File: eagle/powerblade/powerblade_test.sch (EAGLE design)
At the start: 78 parts, among them J1 JTAG_14PIN_IDC-NL, J21 AC_INFILM, Q1 2N7002, U1 TPS62122, U2 AD524, U3 MSP430FR5738, U4 LTC5800, U5 MAX9910, U6 MAX9910

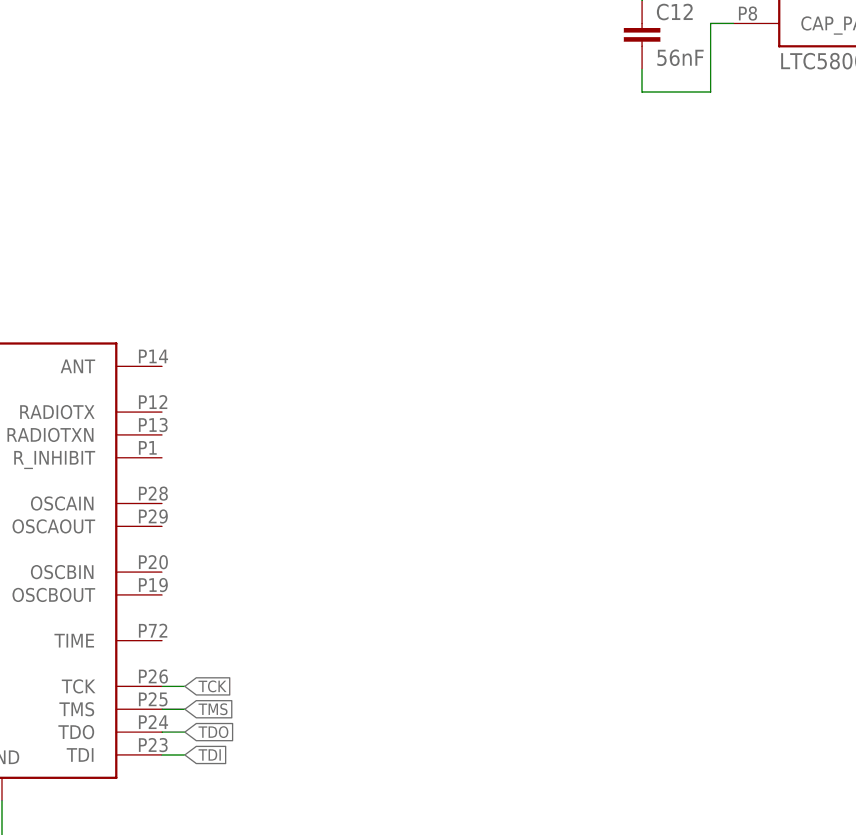
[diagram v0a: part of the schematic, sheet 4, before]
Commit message: added crystals to ltc5800 sch in powerblade test
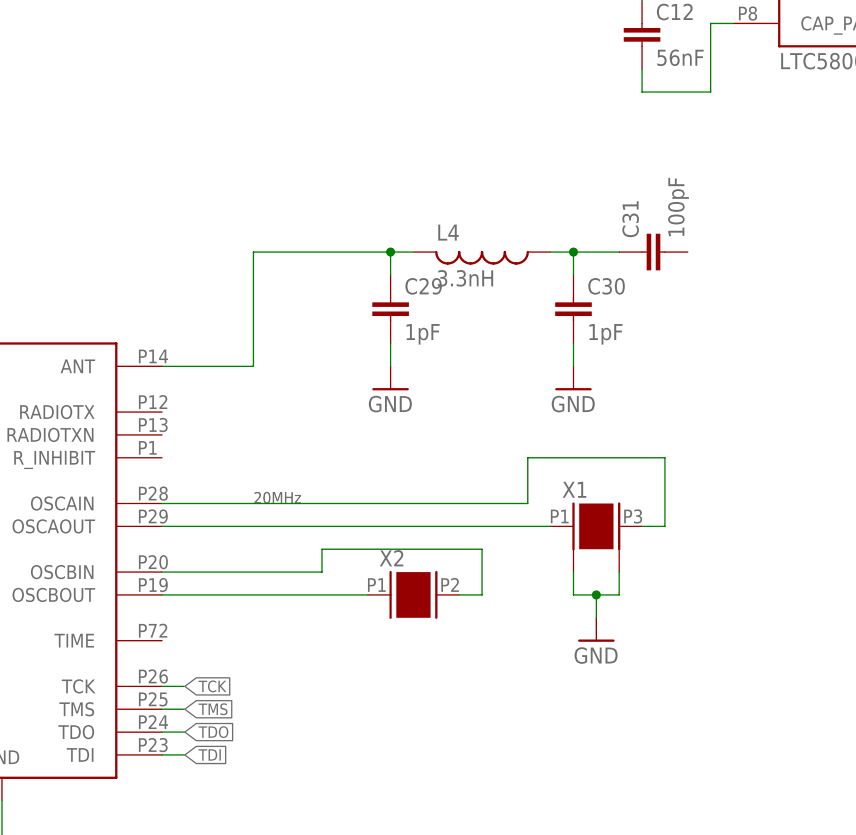
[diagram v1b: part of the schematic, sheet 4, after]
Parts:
- added C29, C30: 1pF, rcl:C-EUC0201
- added C31: 100pF, rcl:C-EUC0201
- added L4: 3.3nH, rcl:L-USL0201
- added X1: ABM8G, powerfilm:ABM8G
- added X2: ABS07, powerfilm:ABS07
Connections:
- new net N$42: U4G$2.OSCAOUT, X1.P1
- new net N$43: U4G$2.OSCAIN, X1.P2
- new net N$44: U4G$2.OSCBIN, X2.P2
- new net N$45: U4G$2.OSCBOUT, X2.P1
- new net N$46: C29.1, L4.2, U4G$2.ANT
- new net N$47: C30.1, C31.1, L4.1
- net GND: now also C29.2, C30.2, X1.G1, X1.G2
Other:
- note added: "20MHz"
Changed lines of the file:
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@@
 <part name="GND32" library="supply1" deviceset="GND" device=""/>
 <part name="+3V9" library="supply1" deviceset="+3V3" device=""/>
+<part name="X1" library="powerfilm" deviceset="ABM8G" device=""/>
+<part name="GND33" library="supply1" deviceset="GND" device=""/>
+<part name="X2" library="powerfilm" deviceset="ABS07" device=""/>
+<part name="L4" library="rcl" deviceset="L-US" device="L0201" value="3.3nH"/>
+<part name="C29" library="rcl" deviceset="C-EU" device="C0201" value="1pF"/>
+<part name="C30" library="rcl" deviceset="C-EU" device="C0201" value="1pF"/>
+<part name="C31" library="rcl" deviceset="C-EU" device="C0201" value="100pF"/>
+<part name="GND34" library="supply1" deviceset="GND" device=""/>
+<part name="GND35" library="supply1" deviceset="GND" device=""/>
 </parts>
 <sheets>
@@
 <description>Load 2: LTC5800</description>
 <plain>
+<text x="27.94" y="0" size="1.27" layer="97">20MHz</text>
 </plain>
 <instances>
@@
 <instance part="GND32" gate="1" x="2.54" y="-93.98"/>
 <instance part="+3V9" gate="G$1" x="-149.86" y="25.4"/>
+<instance part="X1" gate="G$1" x="66.04" y="-2.54"/>
+<instance part="GND33" gate="1" x="66.04" y="-15.24"/>
+<instance part="X2" gate="G$1" x="45.72" y="-10.16"/>
+<instance part="L4" gate="G$1" x="53.34" y="27.94" rot="R270"/>
+<instance part="C29" gate="G$1" x="43.18" y="22.86"/>
+<instance part="C30" gate="G$1" x="63.5" y="22.86"/>
+<instance part="C31" gate="G$1" x="71.12" y="27.94" rot="R90"/>
+<instance part="GND34" gate="1" x="63.5" y="12.7"/>
+<instance part="GND35" gate="1" x="43.18" y="12.7"/>
 </instances>
 <busses>
@@
 <wire x1="-15.24" y1="-81.28" x2="2.54" y2="-81.28" width="0.1524" layer="91"/>
 <wire x1="2.54" y1="-81.28" x2="2.54" y2="-91.44" width="0.1524" layer="91"/>
+</segment>
+<segment>
+<pinref part="X1" gate="G$1" pin="G1"/>
+<wire x1="63.5" y1="-7.62" x2="63.5" y2="-10.16" width="0.1524" layer="91"/>
+<pinref part="X1" gate="G$1" pin="G2"/>
+<wire x1="63.5" y1="-10.16" x2="66.04" y2="-10.16" width="0.1524" layer="91"/>
+<wire x1="66.04" y1="-10.16" x2="68.58" y2="-10.16" width="0.1524" layer="91"/>
+<wire x1="68.58" y1="-10.16" x2="68.58" y2="-7.62" width="0.1524" layer="91"/>
+<pinref part="GND33" gate="1" pin="GND"/>
+<wire x1="66.04" y1="-10.16" x2="66.04" y2="-12.7" width="0.1524" layer="91"/>
+<junction x="66.04" y="-10.16"/>
+</segment>
+<segment>
+<pinref part="C30" gate="G$1" pin="2"/>
+<pinref part="GND34" gate="1" pin="GND"/>
+<wire x1="63.5" y1="17.78" x2="63.5" y2="15.24" width="0.1524" layer="91"/>
+</segment>
+<segment>
+<pinref part="C29" gate="G$1" pin="2"/>
+<pinref part="GND35" gate="1" pin="GND"/>
+<wire x1="43.18" y1="17.78" x2="43.18" y2="15.24" width="0.1524" layer="91"/>
 </segment>
 </net>
@@
 </segment>
 </net>
+<net name="N$42" class="0">
+<segment>
+<pinref part="U4" gate="G$2" pin="OSCAOUT"/>
+<pinref part="X1" gate="G$1" pin="P1"/>
+<wire x1="17.78" y1="-2.54" x2="60.96" y2="-2.54" width="0.1524" layer="91"/>
+</segment>
+</net>
+<net name="N$43" class="0">
+<segment>
+<pinref part="U4" gate="G$2" pin="OSCAIN"/>
+<wire x1="17.78" y1="0" x2="58.42" y2="0" width="0.1524" layer="91"/>
+<wire x1="58.42" y1="0" x2="58.42" y2="5.08" width="0.1524" layer="91"/>
+<wire x1="58.42" y1="5.08" x2="73.66" y2="5.08" width="0.1524" layer="91"/>
+<wire x1="73.66" y1="5.08" x2="73.66" y2="-2.54" width="0.1524" layer="91"/>
+<pinref part="X1" gate="G$1" pin="P2"/>
+<wire x1="73.66" y1="-2.54" x2="71.12" y2="-2.54" width="0.1524" layer="91"/>
+</segment>
+</net>
+<net name="N$44" class="0">
+<segment>
+<pinref part="U4" gate="G$2" pin="OSCBIN"/>
+<wire x1="17.78" y1="-7.62" x2="35.56" y2="-7.62" width="0.1524" layer="91"/>
+<wire x1="35.56" y1="-7.62" x2="35.56" y2="-5.08" width="0.1524" layer="91"/>
+<wire x1="35.56" y1="-5.08" x2="53.34" y2="-5.08" width="0.1524" layer="91"/>
+<wire x1="53.34" y1="-5.08" x2="53.34" y2="-10.16" width="0.1524" layer="91"/>
+<pinref part="X2" gate="G$1" pin="P2"/>
+<wire x1="53.34" y1="-10.16" x2="50.8" y2="-10.16" width="0.1524" layer="91"/>
+</segment>
+</net>
+<net name="N$45" class="0">
+<segment>
+<pinref part="U4" gate="G$2" pin="OSCBOUT"/>
+<pinref part="X2" gate="G$1" pin="P1"/>
+<wire x1="17.78" y1="-10.16" x2="40.64" y2="-10.16" width="0.1524" layer="91"/>
+</segment>
+</net>
+<net name="N$46" class="0">
+<segment>
+<pinref part="U4" gate="G$2" pin="ANT"/>
+<wire x1="17.78" y1="15.24" x2="27.94" y2="15.24" width="0.1524" layer="91"/>
+<wire x1="27.94" y1="15.24" x2="27.94" y2="27.94" width="0.1524" layer="91"/>
+<pinref part="L4" gate="G$1" pin="2"/>
+<wire x1="27.94" y1="27.94" x2="43.18" y2="27.94" width="0.1524" layer="91"/>
+<pinref part="C29" gate="G$1" pin="1"/>
+<wire x1="43.18" y1="27.94" x2="45.72" y2="27.94" width="0.1524" layer="91"/>
+<wire x1="43.18" y1="25.4" x2="43.18" y2="27.94" width="0.1524" layer="91"/>
+<junction x="43.18" y="27.94"/>
+</segment>
+</net>
+<net name="N$47" class="0">
+<segment>
+<pinref part="L4" gate="G$1" pin="1"/>
+<pinref part="C31" gate="G$1" pin="1"/>
+<wire x1="60.96" y1="27.94" x2="63.5" y2="27.94" width="0.1524" layer="91"/>
+<pinref part="C30" gate="G$1" pin="1"/>
+<wire x1="63.5" y1="27.94" x2="68.58" y2="27.94" width="0.1524" layer="91"/>
+<wire x1="63.5" y1="25.4" x2="63.5" y2="27.94" width="0.1524" layer="91"/>
+<junction x="63.5" y="27.94"/>
+</segment>
+</net>

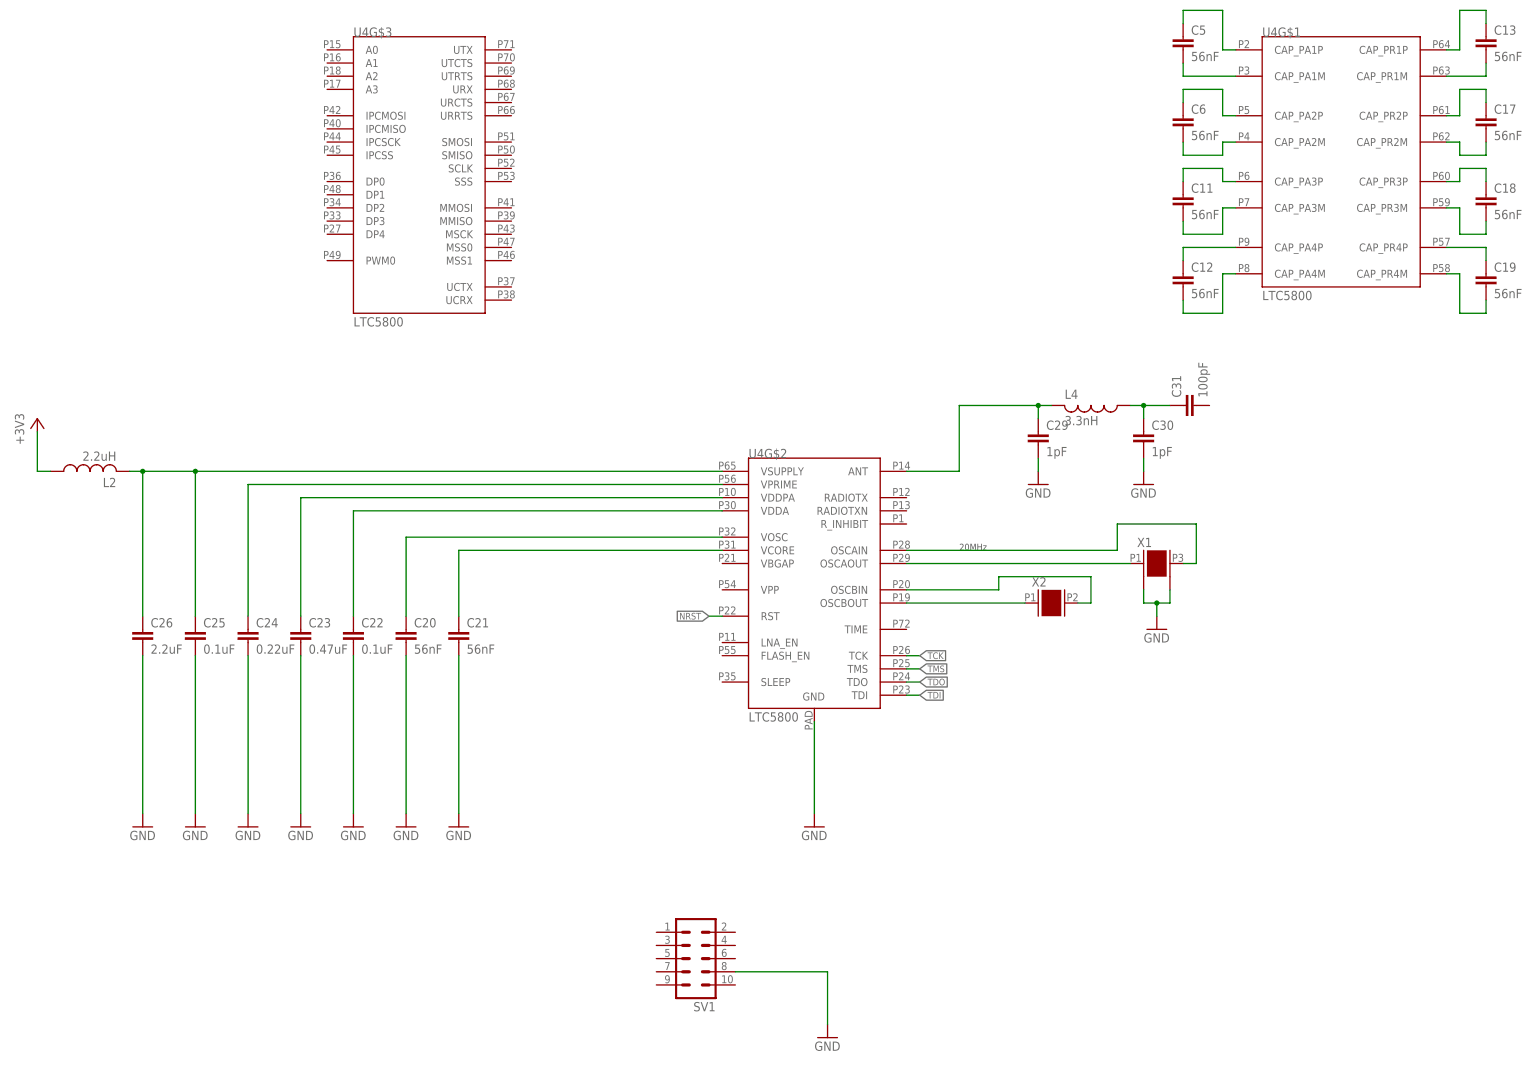
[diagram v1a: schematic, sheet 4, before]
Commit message: added antenna and programming header to ltc5800 schematic
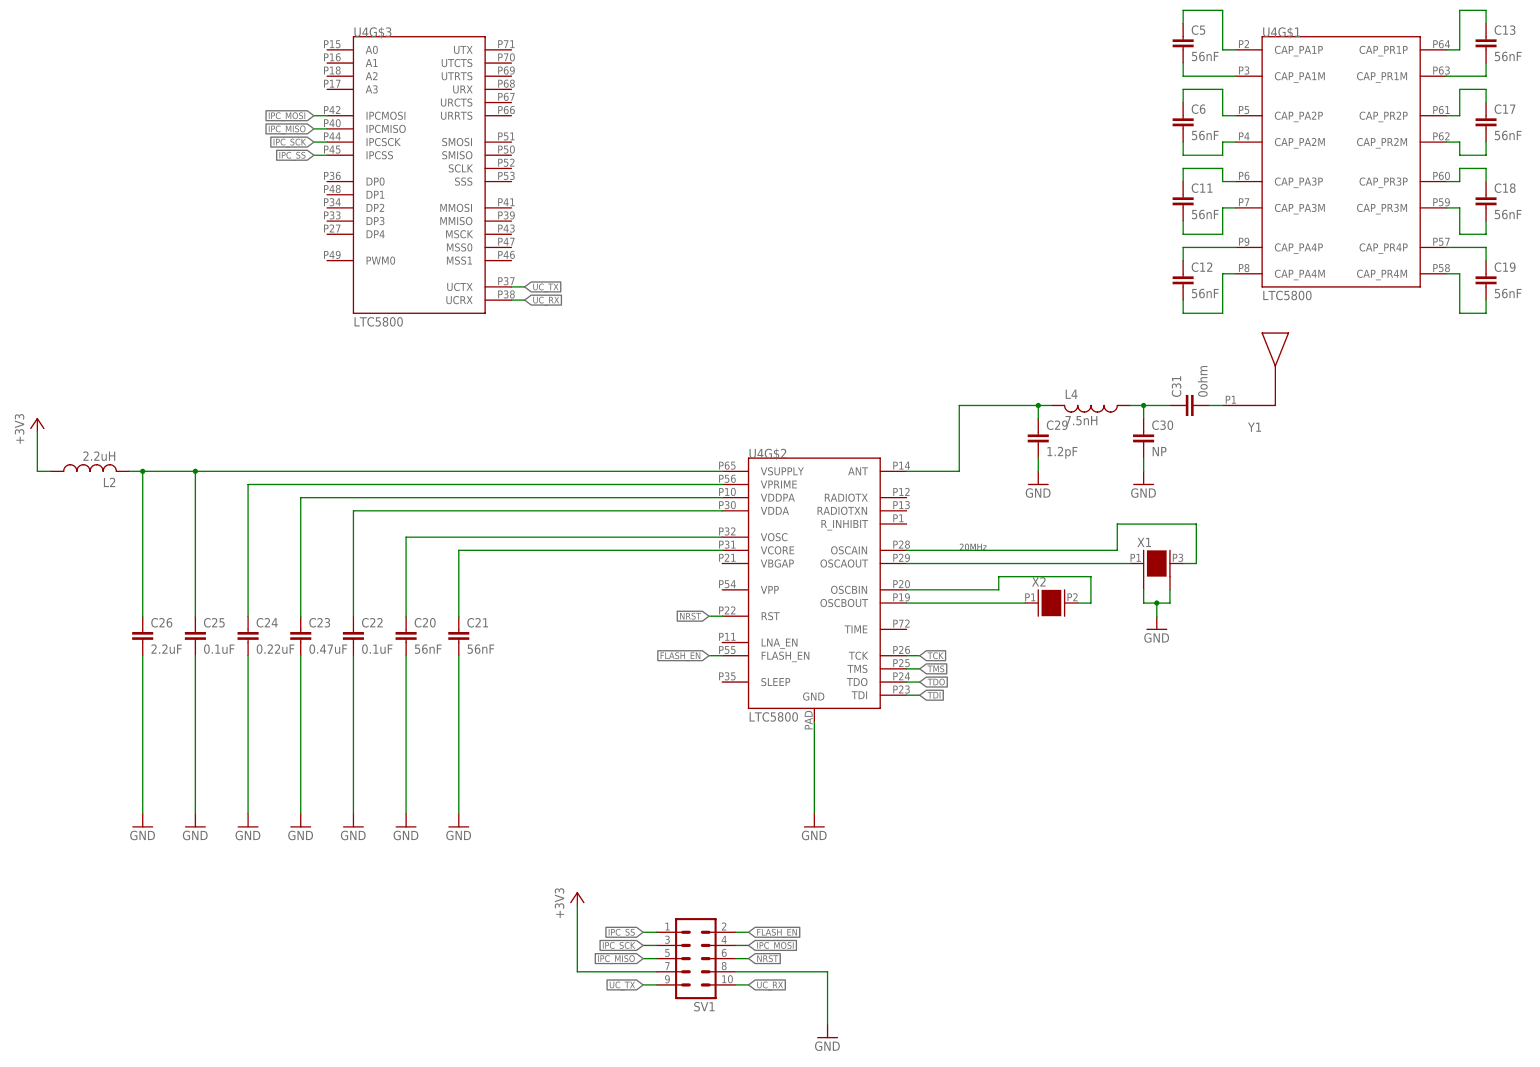
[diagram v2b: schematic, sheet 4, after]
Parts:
- added Y1: UREACH_XTEND, powerfilm:UREACH_XTEND
- C29: value 1pF -> 1.2pF
- C30: value 1pF -> NP
- C31: value 100pF -> 0ohm
- L4: value 3.3nH -> 7.5nH
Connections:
- new net FLASH_EN: SV1.2, U4G$2.FLASH_EN
- new net IPC_MISO: SV1.5, U4G$3.IPCMISO
- new net IPC_MOSI: SV1.4, U4G$3.IPCMOSI
- new net IPC_SCK: SV1.3, U4G$3.IPCSCK
- new net IPC_SS: SV1.1, U4G$3.IPCSS
- new net N$48: C31.2, Y1.P1
- new net UC_RX: SV1.10, U4G$3.UCRX
- new net UC_TX: SV1.9, U4G$3.UCTX
- net +3V3: now also SV1.7
- net NRST: now also SV1.6
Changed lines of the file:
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@@
 <?xml version="1.0" encoding="utf-8"?>
 <!DOCTYPE eagle SYSTEM "eagle.dtd">
-<eagle version="6.5.0">
+<eagle version="6.3">
 <drawing>
 <settings>
@@
 <part name="GND33" library="supply1" deviceset="GND" device=""/>
 <part name="X2" library="powerfilm" deviceset="ABS07" device=""/>
-<part name="L4" library="rcl" deviceset="L-US" device="L0201" value="3.3nH"/>
-<part name="C29" library="rcl" deviceset="C-EU" device="C0201" value="1pF"/>
-<part name="C30" library="rcl" deviceset="C-EU" device="C0201" value="1pF"/>
-<part name="C31" library="rcl" deviceset="C-EU" device="C0201" value="100pF"/>
+<part name="L4" library="rcl" deviceset="L-US" device="L0201" value="7.5nH"/>
+<part name="C29" library="rcl" deviceset="C-EU" device="C0201" value="1.2pF"/>
+<part name="C30" library="rcl" deviceset="C-EU" device="C0201" value="NP"/>
+<part name="C31" library="rcl" deviceset="C-EU" device="C0201" value="0ohm"/>
 <part name="GND34" library="supply1" deviceset="GND" device=""/>
 <part name="GND35" library="supply1" deviceset="GND" device=""/>
+<part name="Y1" library="powerfilm" deviceset="UREACH_XTEND" device=""/>
+<part name="+3V10" library="supply1" deviceset="+3V3" device=""/>
 </parts>
 <sheets>
@@
 <instance part="GND34" gate="1" x="63.5" y="12.7"/>
 <instance part="GND35" gate="1" x="43.18" y="12.7"/>
+<instance part="Y1" gate="G$1" x="88.9" y="27.94" rot="MR0"/>
+<instance part="+3V10" gate="G$1" x="-45.72" y="-66.04"/>
 </instances>
 <busses>
@@
 <label x="-20.32" y="-12.7" size="1.27" layer="95" rot="R180" xref="yes"/>
 </segment>
+<segment>
+<pinref part="SV1" gate="G$1" pin="6"/>
+<wire x1="-12.7" y1="-78.74" x2="-15.24" y2="-78.74" width="0.1524" layer="91"/>
+<label x="-12.7" y="-78.74" size="1.27" layer="95" xref="yes"/>
+</segment>
 </net>
 <net name="TCK" class="0">
@@
 <wire x1="-147.32" y1="15.24" x2="-149.86" y2="15.24" width="0.1524" layer="91"/>
 <wire x1="-149.86" y1="15.24" x2="-149.86" y2="22.86" width="0.1524" layer="91"/>
+</segment>
+<segment>
+<pinref part="+3V10" gate="G$1" pin="+3V3"/>
+<wire x1="-45.72" y1="-68.58" x2="-45.72" y2="-81.28" width="0.1524" layer="91"/>
+<pinref part="SV1" gate="G$1" pin="7"/>
+<wire x1="-45.72" y1="-81.28" x2="-30.48" y2="-81.28" width="0.1524" layer="91"/>
 </segment>
 </net>
@@
 </segment>
 </net>
+<net name="N$48" class="0">
+<segment>
+<pinref part="C31" gate="G$1" pin="2"/>
+<pinref part="Y1" gate="G$1" pin="P1"/>
+<wire x1="76.2" y1="27.94" x2="78.74" y2="27.94" width="0.1524" layer="91"/>
+</segment>
+</net>
+<net name="IPC_SS" class="0">
+<segment>
+<pinref part="SV1" gate="G$1" pin="1"/>
+<wire x1="-33.02" y1="-73.66" x2="-30.48" y2="-73.66" width="0.1524" layer="91"/>
+<label x="-33.02" y="-73.66" size="1.27" layer="95" rot="R180" xref="yes"/>
+</segment>
+<segment>
+<pinref part="U4" gate="G$3" pin="IPCSS"/>
+<wire x1="-96.52" y1="76.2" x2="-93.98" y2="76.2" width="0.1524" layer="91"/>
+<label x="-96.52" y="76.2" size="1.27" layer="95" rot="R180" xref="yes"/>
+</segment>
+</net>
+<net name="IPC_SCK" class="0">
+<segment>
+<pinref part="SV1" gate="G$1" pin="3"/>
+<wire x1="-33.02" y1="-76.2" x2="-30.48" y2="-76.2" width="0.1524" layer="91"/>
+<label x="-33.02" y="-76.2" size="1.27" layer="95" rot="R180" xref="yes"/>
+</segment>
+<segment>
+<pinref part="U4" gate="G$3" pin="IPCSCK"/>
+<wire x1="-96.52" y1="78.74" x2="-93.98" y2="78.74" width="0.1524" layer="91"/>
+<label x="-96.52" y="78.74" size="1.27" layer="95" rot="R180" xref="yes"/>
+</segment>
+</net>
+<net name="IPC_MISO" class="0">
+<segment>
+<pinref part="SV1" gate="G$1" pin="5"/>
+<wire x1="-33.02" y1="-78.74" x2="-30.48" y2="-78.74" width="0.1524" layer="91"/>
+<label x="-33.02" y="-78.74" size="1.27" layer="95" rot="R180" xref="yes"/>
+</segment>
+<segment>
+<pinref part="U4" gate="G$3" pin="IPCMISO"/>
+<wire x1="-96.52" y1="81.28" x2="-93.98" y2="81.28" width="0.1524" layer="91"/>
+<label x="-96.52" y="81.28" size="1.27" layer="95" rot="R180" xref="yes"/>
+</segment>
+</net>
+<net name="UC_TX" class="0">
+<segment>
+<pinref part="SV1" gate="G$1" pin="9"/>
+<wire x1="-33.02" y1="-83.82" x2="-30.48" y2="-83.82" width="0.1524" layer="91"/>
+<label x="-33.02" y="-83.82" size="1.27" layer="95" rot="R180" xref="yes"/>
+</segment>
+<segment>
+<pinref part="U4" gate="G$3" pin="UCTX"/>
+<wire x1="-55.88" y1="50.8" x2="-58.42" y2="50.8" width="0.1524" layer="91"/>
+<label x="-55.88" y="50.8" size="1.27" layer="95" xref="yes"/>
+</segment>
+</net>
+<net name="FLASH_EN" class="0">
+<segment>
+<pinref part="SV1" gate="G$1" pin="2"/>
+<wire x1="-12.7" y1="-73.66" x2="-15.24" y2="-73.66" width="0.1524" layer="91"/>
+<label x="-12.7" y="-73.66" size="1.27" layer="95" xref="yes"/>
+</segment>
+<segment>
+<pinref part="U4" gate="G$2" pin="FLASH_EN"/>
+<wire x1="-20.32" y1="-20.32" x2="-17.78" y2="-20.32" width="0.1524" layer="91"/>
+<label x="-20.32" y="-20.32" size="1.27" layer="95" rot="R180" xref="yes"/>
+</segment>
+</net>
+<net name="IPC_MOSI" class="0">
+<segment>
+<pinref part="SV1" gate="G$1" pin="4"/>
+<wire x1="-12.7" y1="-76.2" x2="-15.24" y2="-76.2" width="0.1524" layer="91"/>
+<label x="-12.7" y="-76.2" size="1.27" layer="95" xref="yes"/>
+</segment>
+<segment>
+<pinref part="U4" gate="G$3" pin="IPCMOSI"/>
+<wire x1="-96.52" y1="83.82" x2="-93.98" y2="83.82" width="0.1524" layer="91"/>
+<label x="-96.52" y="83.82" size="1.27" layer="95" rot="R180" xref="yes"/>
+</segment>
+</net>
+<net name="UC_RX" class="0">
+<segment>
+<pinref part="SV1" gate="G$1" pin="10"/>
+<wire x1="-12.7" y1="-83.82" x2="-15.24" y2="-83.82" width="0.1524" layer="91"/>
+<label x="-12.7" y="-83.82" size="1.27" layer="95" xref="yes"/>
+</segment>
+<segment>
+<pinref part="U4" gate="G$3" pin="UCRX"/>
+<wire x1="-55.88" y1="48.26" x2="-58.42" y2="48.26" width="0.1524" layer="91"/>
+<label x="-55.88" y="48.26" size="1.27" layer="95" xref="yes"/>
+</segment>
+</net>
